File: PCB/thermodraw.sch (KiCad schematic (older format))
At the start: 36 parts, among them CON1 BARREL_JACK, J1 CONN-10-DIL, P1 Molex 47053-1000, Q1 DMP3098L, Q2 DMP3098L, Q3 DMP3098L, SW1 T_UP, SW2 T_DOWN, SW3 RESET, U1 TPS71533DCKR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

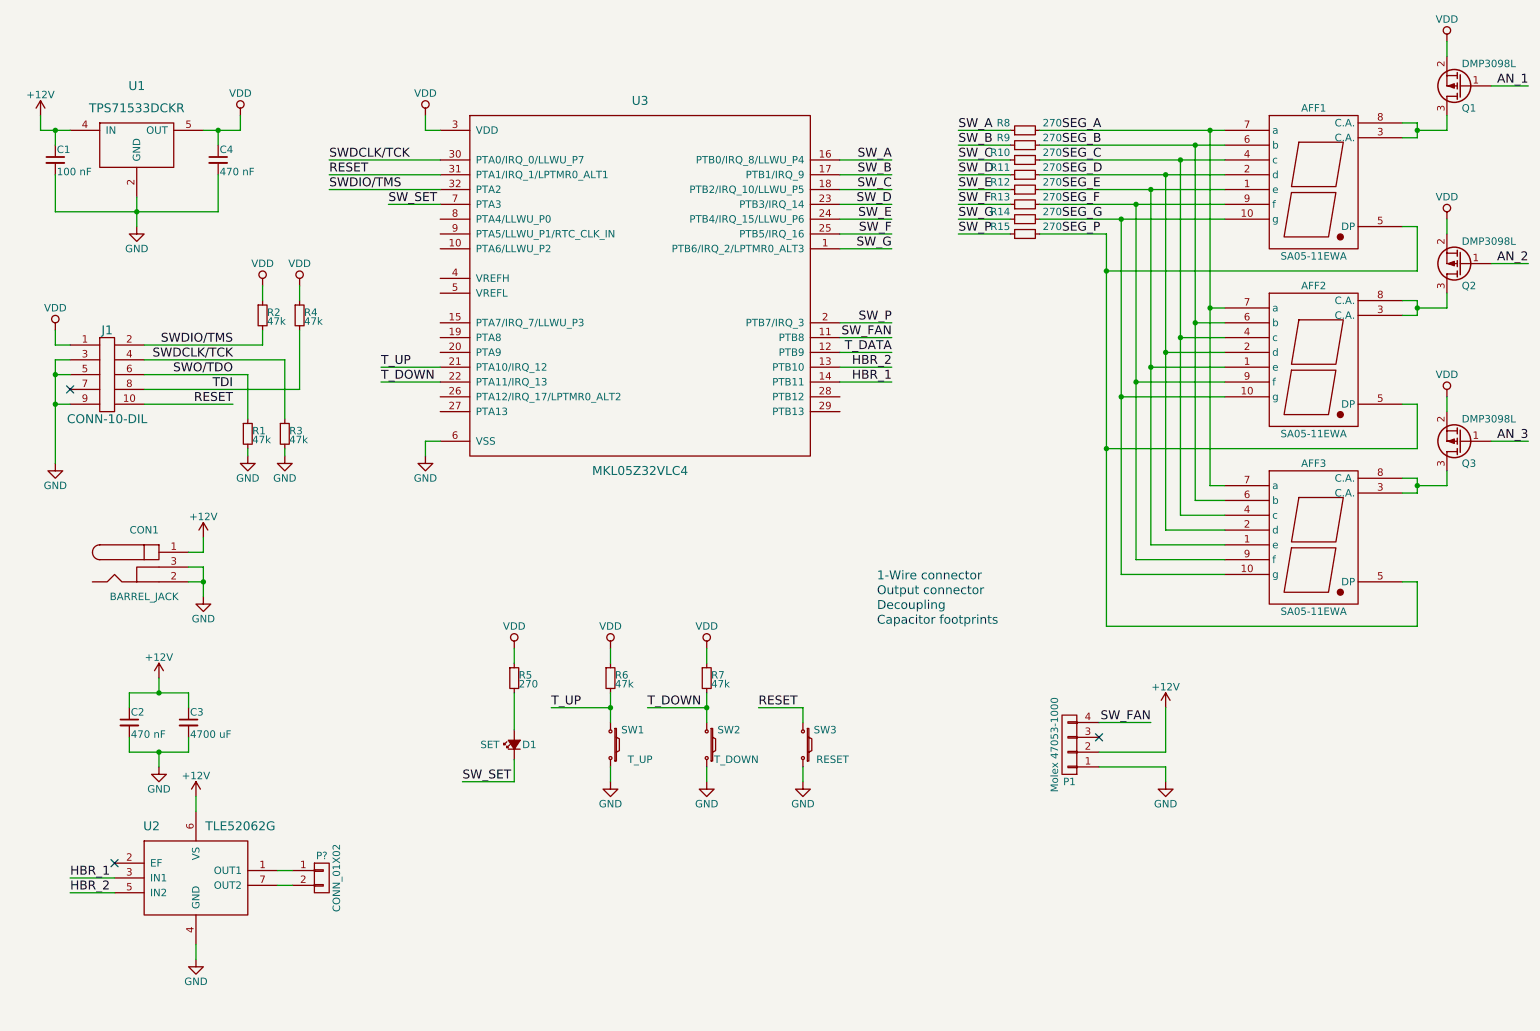
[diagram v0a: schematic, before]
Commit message: Added capacitor footprints.
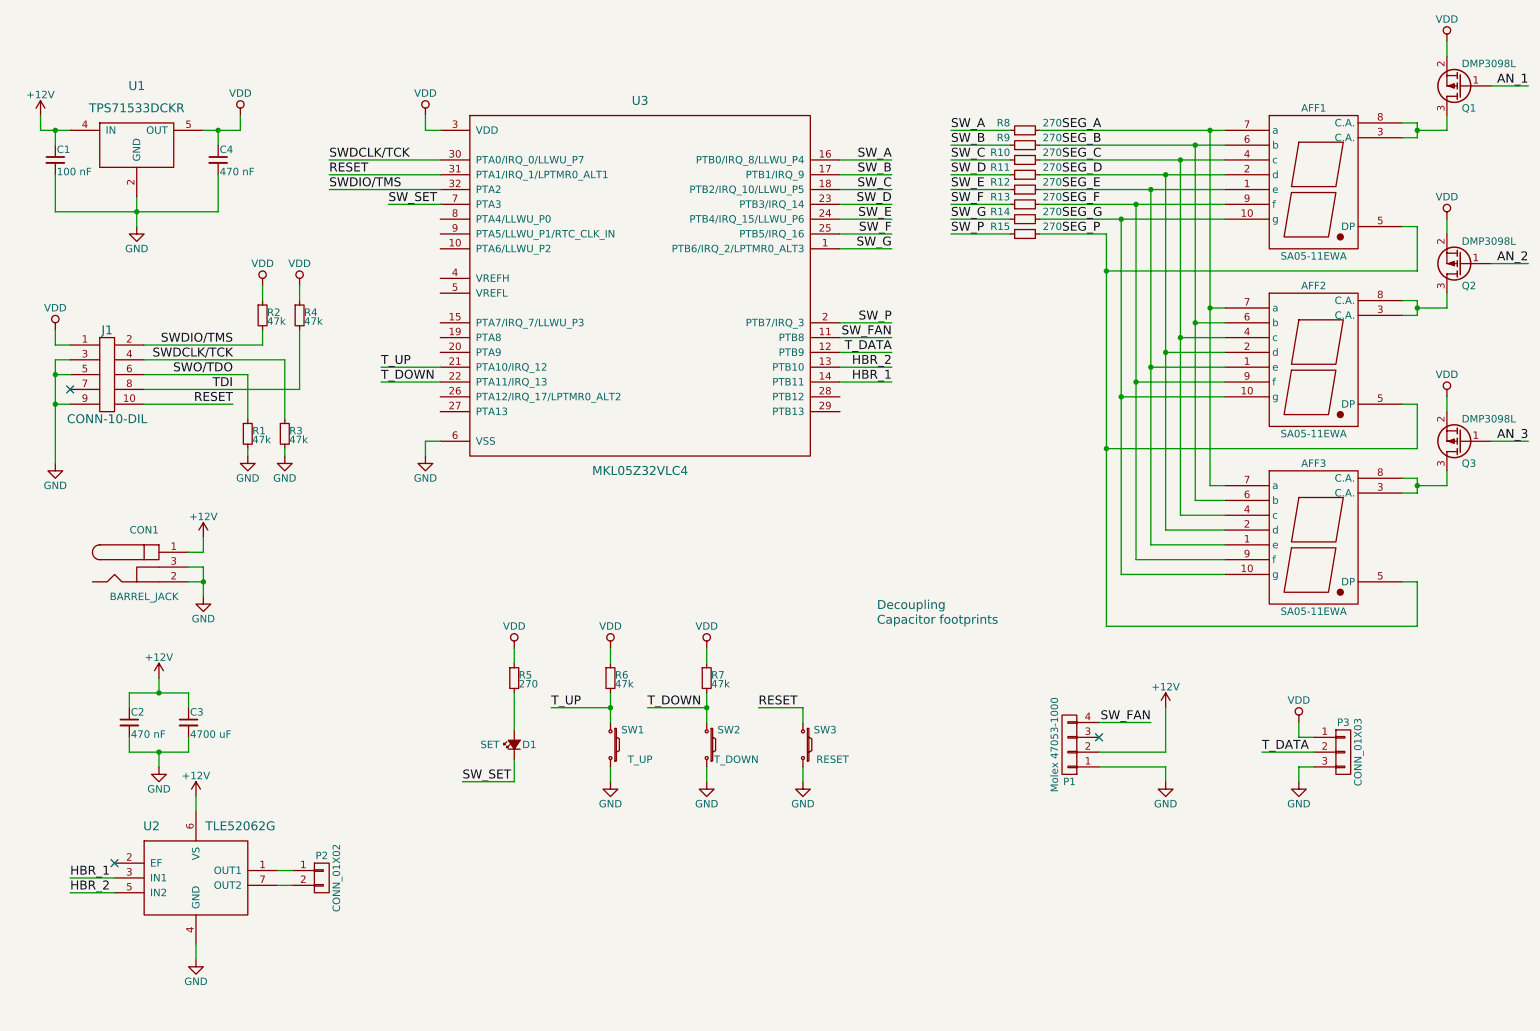
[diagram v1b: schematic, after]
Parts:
- added P3: CONN_01X03, symbol CONN_01X03
- C1, C2, C4: footprint (none) -> Capacitors_SMD:C_0603_HandSoldering
- gave numbers to parts that had none: 1
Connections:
- net GND: now also P3.3 (P3)
- net T_DATA: now also P3.2 (P2)
- net VDD: now also P3.1 (P1)
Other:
- note removed: "1-Wire connector"
- note removed: "Output connector"

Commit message: Finished routing, added pours.
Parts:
- added C5, C6: 1500 uF, Custom:c_elec_18x22, symbol C_Small
- added C7: 100 nF, Capacitors_SMD:C_0603_HandSoldering, symbol C_Small
- added D2: CUS520,H3F, Diodes_SMD:SOD-323, symbol D_Schottky_Small
- added R16: 47k, Resistors_SMD:R_0603_HandSoldering, symbol R_Small
- C3: value 4700 uF -> 1500 uF; footprint (none) -> Custom:c_elec_18x22; Digikey part no. (none) -> 1189-3575-2-ND
- D1: footprint (none) -> LEDs:LED_0603
- P2: footprint (none) -> Terminal_Blocks:TerminalBlock_Pheonix_MKDS1.5-2pol
- P3: footprint (none) -> Terminal_Blocks:TerminalBlock_Pheonix_MKDS1.5-3pol
- SW1: footprint (none) -> Buttons_Switches_SMD:SW_SPST_PTS645; Digikey part no. (none) -> CKN9087CT-ND
- SW2, SW3: footprint (none) -> Buttons_Switches_SMD:SW_SPST_PTS645
- U2: footprint (none) -> Custom:TO-263-7Lead
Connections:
- net +12V: now also C5.1, C6.1
- net AN_1: now also U3.15 (PTA7/IRQ_7/LLWU_P3)
- net AN_2: now also U3.19 (PTA8)
- net AN_3: now also U3.20 (PTA9)
- net GND: now also U3.5 (VREFL), C5.2, C6.2, C7.2
- net RESET: now also R16.2
- net SW_FAN: now also D2.2 (A)
- net VDD: now also U3.4 (VREFH), C7.1, D2.1 (K), R16.1
- net AN_2_PWR: now reaches AFF2.3 (C.A.), AFF2.8 (C.A.), Q2.3 (D)
- net AN_1_PWR: now reaches AFF1.3 (C.A.), AFF1.8 (C.A.), Q1.3 (D)
- net AN_3_PWR: now reaches AFF3.3 (C.A.), AFF3.8 (C.A.), Q3.3 (D)
- net HBR_OUT1: now reaches P2.1 (P1), U2.1 (OUT1)
- net EF: now reaches U2.2 (EF)
- net HBR_OUT2: now reaches P2.2 (P2), U2.7 (OUT2)
- net SET_AN: now reaches D1.2 (A), R5.2
- no-connect marks 3 -> 10
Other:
- note removed: "Capacitor footprints"
- note removed: "Decoupling"
- moved on the sheet: C2, C3, J1, P2, R1, R2, R3, R4, U2
